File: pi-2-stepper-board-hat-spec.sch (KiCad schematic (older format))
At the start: 36 parts, among them CON1 DC12v, P1 Servo, P10 BK_FEED_BYPASS, P2 Endstop1, P3 Endstop2, P4 Stepper1, P5 Stepper2, P6 COM, P7 Aux1 (SPI), P8 Aux2 (I2C)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

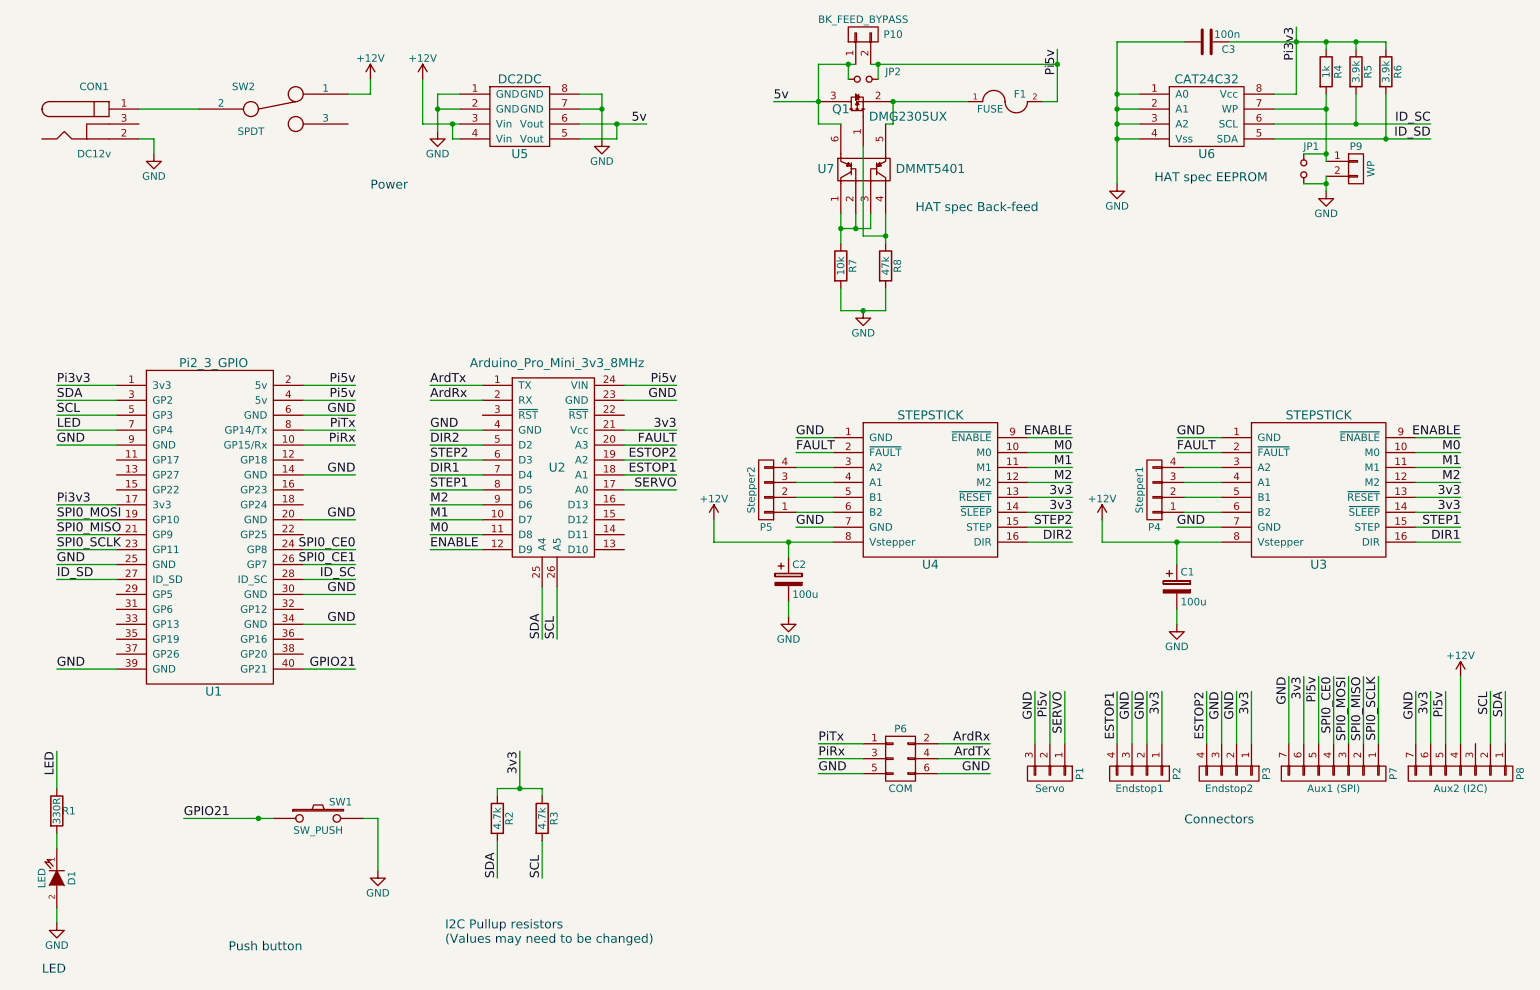
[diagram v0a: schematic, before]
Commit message: Milestone 1.01b fixes
Swapped com port sides
Replaced LED with Bi-colour LED
Fixed Silkscreen & NPTH plated slot
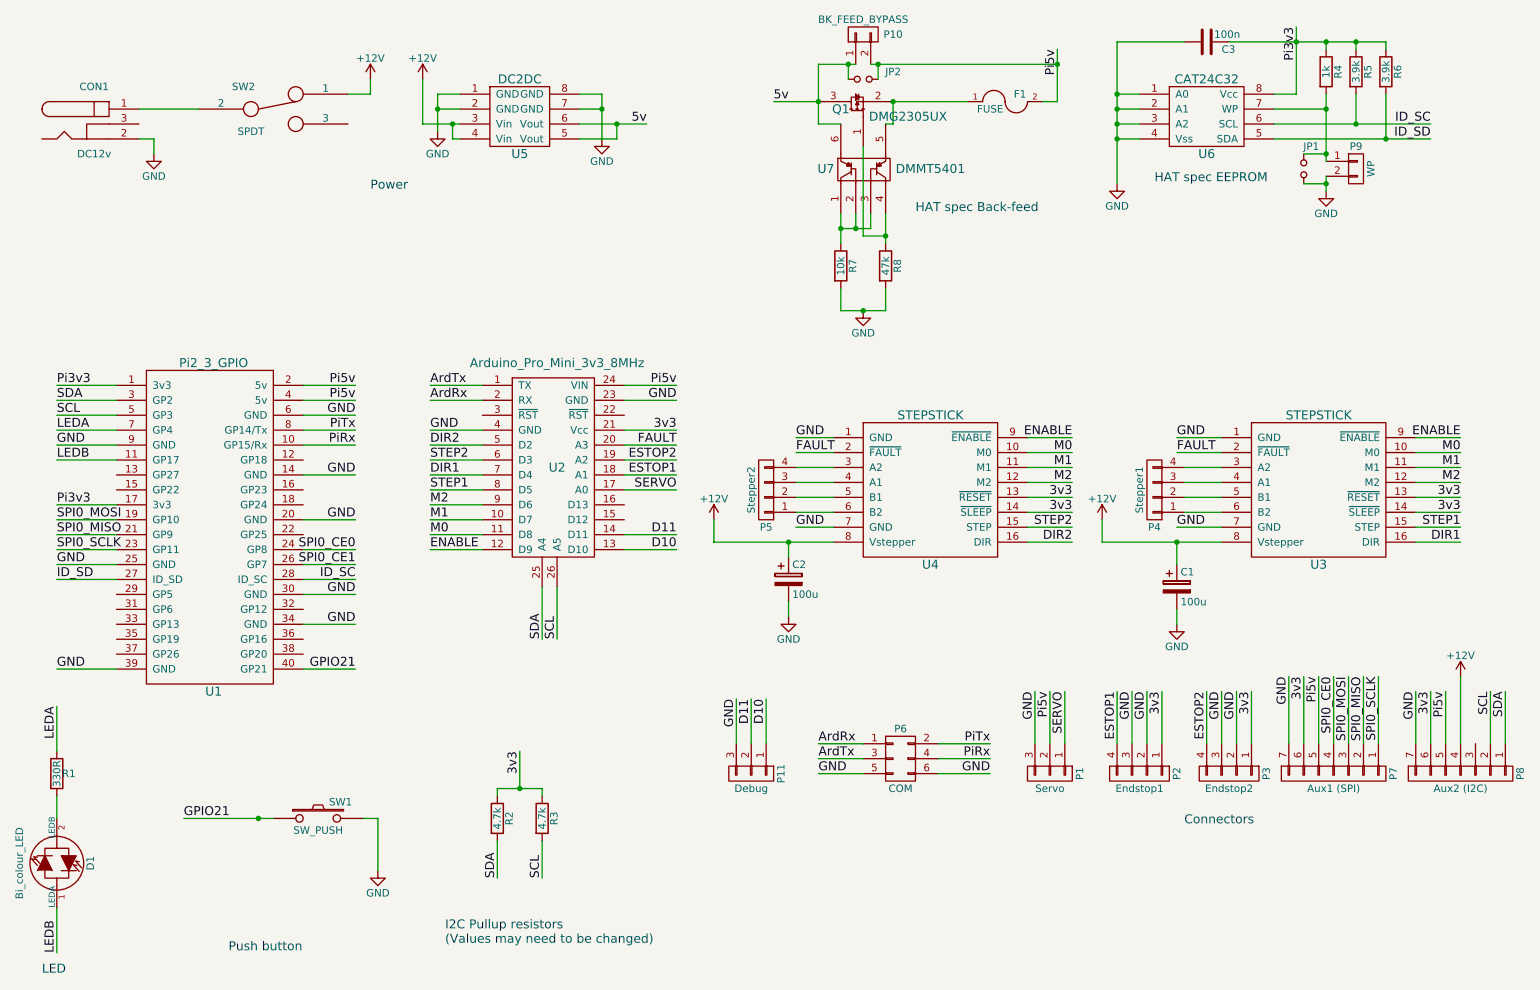
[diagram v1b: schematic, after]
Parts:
- removed D1: LED, LEDs:LED-3MM, symbol LED
- added D1: Bi_colour_LED, LEDs:LED-3MM, symbol Bi_colour_LED
- added P11: Debug, symbol CONN_01X03
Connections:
- net ArdRx: now also P6.1 (P1); no longer P6.2 (P2)
- net ArdTx: now also P6.3 (P3); no longer P6.4 (P4)
- net GND: now also P11.3 (P3)
- net PiRx: now also P6.4 (P4); no longer P6.3 (P3)
- net PiTx: now also P6.2 (P2); no longer P6.1 (P1)
- net LEDB: now reaches U1.11 (GP17)
- net LEDB: now also D1.1 (LEDA)
- net D10: now reaches U2.13 (D10)
- net D10: now also P11.1 (P1)
- net D11: now reaches U2.14 (D11)
- net D11: now also P11.2 (P2)
- net at R1.2: now also D1.2 (LEDB)
- net LED renamed LEDA
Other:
- moved on the sheet: R1
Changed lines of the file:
@@
 Sheet 1 1
 Title "Pi 2/3 Arduino Stepper board"
-Date "2016-04-06"
-Rev "1"
+Date "2016-04-24"
+Rev "1.01b"
 Comp ""
 Comment1 "Copyright Mark Benson 2016"
@@
 Text Label 1250 3900 0    60   ~ 0
 GND
-Text Label 6350 5900 0    60   ~ 0
+Text Label 7500 5900 2    60   ~ 0
 PiTx
-Text Label 6350 6000 0    60   ~ 0
+Text Label 7500 6000 2    60   ~ 0
 PiRx
 Text Label 3250 3800 2    60   ~ 0
@@
 Text Label 3750 3600 0    60   ~ 0
 ArdRx
-Text Label 7500 6000 2    60   ~ 0
+Text Label 6350 6000 0    60   ~ 0
 ArdTx
-Text Label 7500 5900 2    60   ~ 0
+Text Label 6350 5900 0    60   ~ 0
 ArdRx
 Text Label 8450 5550 3    60   ~ 0
@@
 	6150 4950 6150 5050
 Wire Wire Line
-	4900 1850 4900 1550
+	4900 1550 4900 1850
 Wire Wire Line
 	4900 1550 4750 1550
@@
 Connection ~ 3800 1650
 Wire Wire Line
-	3950 1750 3700 1750
+	3700 1750 3950 1750
 Wire Wire Line
 	3700 1750 3700 1450
@@
 $EndComp
 Wire Wire Line
-	4500 6250 4500 6200
-Wire Wire Line
-	4500 6200 4200 6200
+	4500 6200 4500 6250
+Wire Wire Line
+	4200 6200 4500 6200
 Wire Wire Line
 	4200 6200 4200 6250
@@
 	1650 4300 1250 4300
 Wire Wire Line
-	9400 1550 9550 1550
-Wire Wire Line
-	9550 1550 9550 1100
+	9550 1550 9400 1550
+Wire Wire Line
+	9550 1100 9550 1550
 Text Label 9550 1100 3    60   ~ 0
 Pi3v3
@@
 $EndComp
 Wire Wire Line
-	6500 2550 6500 2350
-Wire Wire Line
-	6800 2550 6800 2350
-Wire Wire Line
-	6700 2350 6700 2450
-Wire Wire Line
-	6700 2450 6500 2450
+	6500 2350 6500 2550
+Wire Wire Line
+	6800 2350 6800 2550
+Wire Wire Line
+	6700 2450 6700 2350
+Wire Wire Line
+	6500 2450 6700 2450
 Connection ~ 6500 2450
 Wire Wire Line
@@
 	6350 1350 6600 1350
 Wire Wire Line
-	7850 1600 7950 1600
-Wire Wire Line
-	7950 1600 7950 1250
+	7950 1600 7850 1600
+Wire Wire Line
+	7950 1250 7950 1600
 Wire Wire Line
 	6850 1750 6850 1600
@@
 Pi5v
 $Comp
-L LED D1
-U 1 1 57040A56
-P 1250 6800
-F 0 "D1" H 1250 6900 50  0000 C CNN
-F 1 "LED" H 1250 6700 50  0000 C CNN
-F 2 "LEDs:LED-3MM" H 1250 6800 50  0001 C CNN
-F 3 "" H 1250 6800 50  0000 C CNN
-	1    1250 6800
-	0    1    1    0
-$EndComp
-$Comp
-L GND #PWR015
-U 1 1 57040C64
-P 1250 7100
-F 0 "#PWR015" H 1250 6850 50  0001 C CNN
-F 1 "GND" H 1250 6950 50  0000 C CNN
-F 2 "" H 1250 7100 50  0000 C CNN
-F 3 "" H 1250 7100 50  0000 C CNN
-	1    1250 7100
-	1    0    0    -1
-$EndComp
-$Comp
 L R R1
 U 1 1 57040CFB
-P 1250 6350
-F 0 "R1" H 1330 6350 50  0000 C CNN
-F 1 "330R" V 1250 6350 50  0000 C CNN
-F 2 "Discret:R1" V 1180 6350 50  0001 C CNN
-F 3 "" H 1250 6350 50  0000 C CNN
-	1    1250 6350
-	1    0    0    -1
-$EndComp
-Wire Wire Line
-	1250 6600 1250 6500
-Wire Wire Line
-	1250 7000 1250 7100
+P 1250 6100
+F 0 "R1" H 1330 6100 50  0000 C CNN
+F 1 "330R" V 1250 6100 50  0000 C CNN
+F 2 "Discret:R1" V 1180 6100 50  0001 C CNN
+F 3 "" H 1250 6100 50  0000 C CNN
+	1    1250 6100
+	1    0    0    -1
+$EndComp
 Wire Wire Line
 	1650 3800 1250 3800
 Text Label 1250 3800 0    60   ~ 0
-LED
-Text Label 1250 5950 3    60   ~ 0
-LED
-Wire Wire Line
-	1250 6200 1250 5950
+LEDA
+Text Label 1250 5650 3    60   ~ 0
+LEDA
 Text Notes 1150 7450 0    60   ~ 0
 LED
 Text Notes 7000 2350 0    60   ~ 0
 HAT spec Back-feed
+Wire Wire Line
+	1650 4000 1250 4000
+Text Label 1250 4000 0    60   ~ 0
+LEDB
+Wire Wire Line
+	1250 7000 1250 7300
+Text Label 1250 7300 1    60   ~ 0
+LEDB
+$Comp
+L Bi_colour_LED D1
+U 1 1 571CBDC5
+P 1250 6700
+F 0 "D1" H 1250 6925 50  0000 C CNN
+F 1 "Bi_colour_LED" H 1250 6450 50  0000 C CNN
+F 2 "LEDs:LED-3MM" H 1250 6700 50  0001 C CNN
+F 3 "" H 1250 6700 50  0000 C CNN
+	1    1250 6700
+	0    1    1    0
+$EndComp
+Wire Wire Line
+	1250 6400 1250 6250
+Wire Wire Line
+	1250 5950 1250 5650
+$Comp
+L CONN_01X03 P11
+U 1 1 571CEBE9
+P 5900 6100
+F 0 "P11" H 5900 6300 50  0000 C CNN
+F 1 "Debug" V 6000 6100 50  0000 C CNN
+F 2 "" H 5900 6100 50  0000 C CNN
+F 3 "" H 5900 6100 50  0000 C CNN
+	1    5900 6100
+	0    1    1    0
+$EndComp
+Wire Wire Line
+	5800 5900 5800 5600
+Wire Wire Line
+	5900 5900 5900 5600
+Wire Wire Line
+	6000 5900 6000 5600
+Text Label 6000 5600 3    60   ~ 0
+D10
+Text Label 5900 5600 3    60   ~ 0
+D11
+Text Label 5800 5600 3    60   ~ 0
+GND
+Wire Wire Line
+	5050 4600 5400 4600
+Wire Wire Line
+	5050 4500 5400 4500
+Text Label 5400 4600 2    60   ~ 0
+D10
+Text Label 5400 4500 2    60   ~ 0
+D11
 $EndSCHEMATC

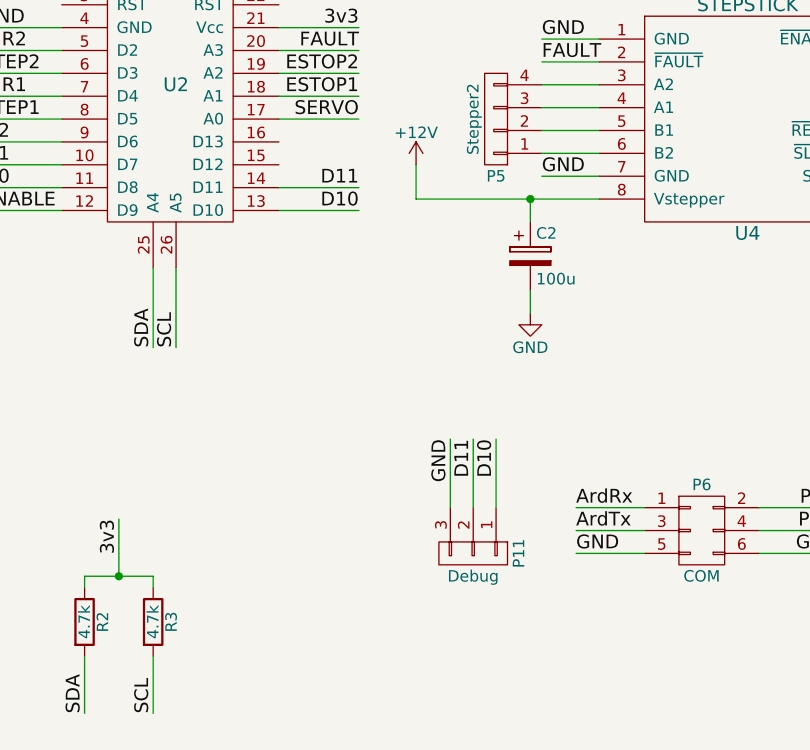
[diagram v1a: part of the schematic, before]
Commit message: Clean up schematic
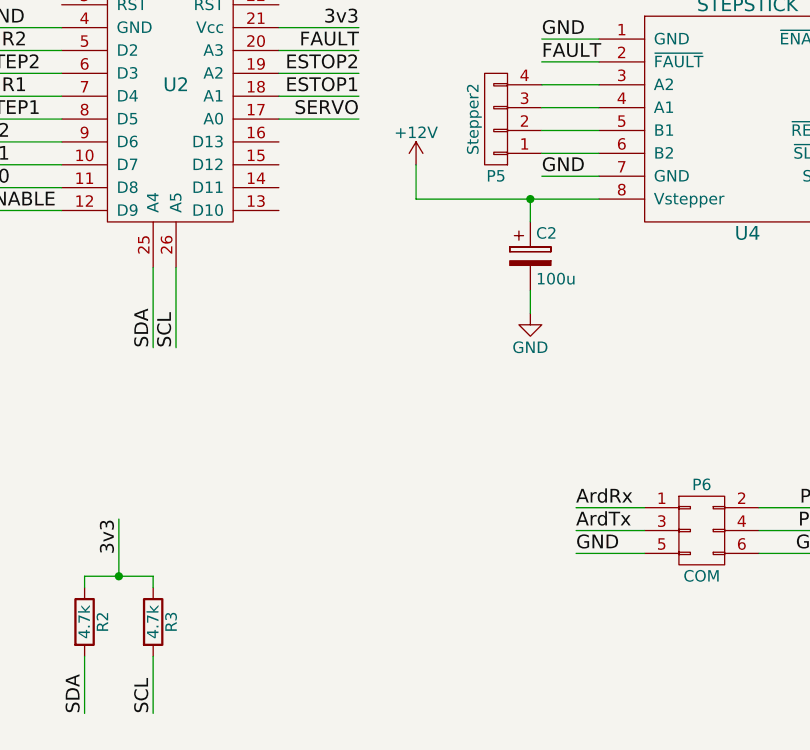
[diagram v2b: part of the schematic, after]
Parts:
- removed P11: Debug, symbol CONN_01X03
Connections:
- net D10: no longer names the net of U2.13 (D10)
- net D11: no longer names the net of U2.14 (D11)
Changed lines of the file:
@@
 Wire Wire Line
 	1250 5950 1250 5650
-$Comp
-L CONN_01X03 P11
-U 1 1 571CEBE9
-P 5900 6100
-F 0 "P11" H 5900 6300 50  0000 C CNN
-F 1 "Debug" V 6000 6100 50  0000 C CNN
-F 2 "" H 5900 6100 50  0000 C CNN
-F 3 "" H 5900 6100 50  0000 C CNN
-	1    5900 6100
-	0    1    1    0
-$EndComp
-Wire Wire Line
-	5800 5900 5800 5600
-Wire Wire Line
-	5900 5900 5900 5600
-Wire Wire Line
-	6000 5900 6000 5600
-Text Label 6000 5600 3    60   ~ 0
-D10
-Text Label 5900 5600 3    60   ~ 0
-D11
-Text Label 5800 5600 3    60   ~ 0
-GND
-Wire Wire Line
-	5050 4600 5400 4600
-Wire Wire Line
-	5050 4500 5400 4500
-Text Label 5400 4600 2    60   ~ 0
-D10
-Text Label 5400 4500 2    60   ~ 0
-D11
 $EndSCHEMATC
